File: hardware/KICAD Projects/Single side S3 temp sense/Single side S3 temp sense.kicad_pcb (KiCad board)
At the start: 2 copper layers, 39 parts, among them J1 TYPE-C-31-M-12, J2 DTF13-6P, SW1 PTS810_SJM_250_SMTR_LFS, SW2 PTS810_SJM_250_SMTR_LFS, U1 AMS1117-3.3, U2 ESP32-S3-WROOM-1, U3 MCP2515-I, U4 TJA1050DRG, X1 8MHz

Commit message: can template finished
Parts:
- removed D6: SK6812, LED_SMD:LED_SK6812_PLCC4_5.0x5.0mm_P3.2mm
- added REF**: MountingHole_3.2mm_M3, MountingHole:MountingHole_3.2mm_M3, F.Cu at (147.5, 102.5)
- added REF**: MountingHole_3.2mm_M3, MountingHole:MountingHole_3.2mm_M3, F.Cu at (87.9, 57.4)
- added REF**: MountingHole_3.2mm_M3, MountingHole:MountingHole_3.2mm_M3, F.Cu at (87.9, 103.6)
- added REF**: MountingHole_3.2mm_M3, MountingHole:MountingHole_3.2mm_M3, F.Cu at (147.5, 58.5)
- U5: moved to B.Cu
- moved R9 153.0 mm to (114.2, 69.5)
- moved R4 149.1 mm to (114.2, 71.2)
- moved C8 144.9 mm to (114.2, 68.0), turned to 180 degrees
- moved C7 144.9 mm to (114.2, 66.2), turned to 180 degrees
- moved C6 141.0 mm to (114.2, 72.8), turned to 180 degrees
- moved U2 123.6 mm to (126.1, 69.3)
- moved R6 122.9 mm to (138.8, 70.7), turned to 90 degrees
- moved C10 122.2 mm to (138.8, 67.2), turned to 90 degrees
- moved C11 122.0 mm to (116.2, 89.8), turned to 180 degrees
- moved U3 118.7 mm to (123.8, 96.8)
- moved R8 118.0 mm to (123.1, 89.5)
- moved R5 116.8 mm to (138.8, 78.5), turned to 90 degrees
- moved SW2 116.5 mm to (142.1, 69.0), turned to -90 degrees
- moved C9 115.3 mm to (138.8, 75.2), turned to 90 degrees
- moved SW1 111.3 mm to (142.1, 76.8), turned to -90 degrees
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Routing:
- net VCC_3V3: track 0.00 -> 94.7 mm, vias 0 -> 4
- net VCC_5V: track 0.00 -> 81.4 mm, vias 0 -> 2
- net GND: track 0.00 -> 80.7 mm, vias 0 -> 18
- net High: track 0.00 -> 78.9 mm
- net Low: track 0.00 -> 68.8 mm
- net SCL: track 0.00 -> 43.1 mm
- net CHIP_PU: track 0.00 -> 41.4 mm, vias 0 -> 3
- net Net-(U3-OSC2): track 0.00 -> 28.1 mm
- net SCK: track 0.00 -> 26.6 mm, vias 0 -> 2
- net D+: track 0.00 -> 25.4 mm
- net D-: track 0.00 -> 25.3 mm
- net SDA: track 0.00 -> 24.2 mm
- net Net-(U3-TXCAN): track 0.00 -> 23.7 mm
- net Net-(D1-A): track 0.00 -> 22.9 mm
- net Net-(U3-OSC1): track 0.00 -> 22.3 mm
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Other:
- board outline added: 78.9 x 54 mm

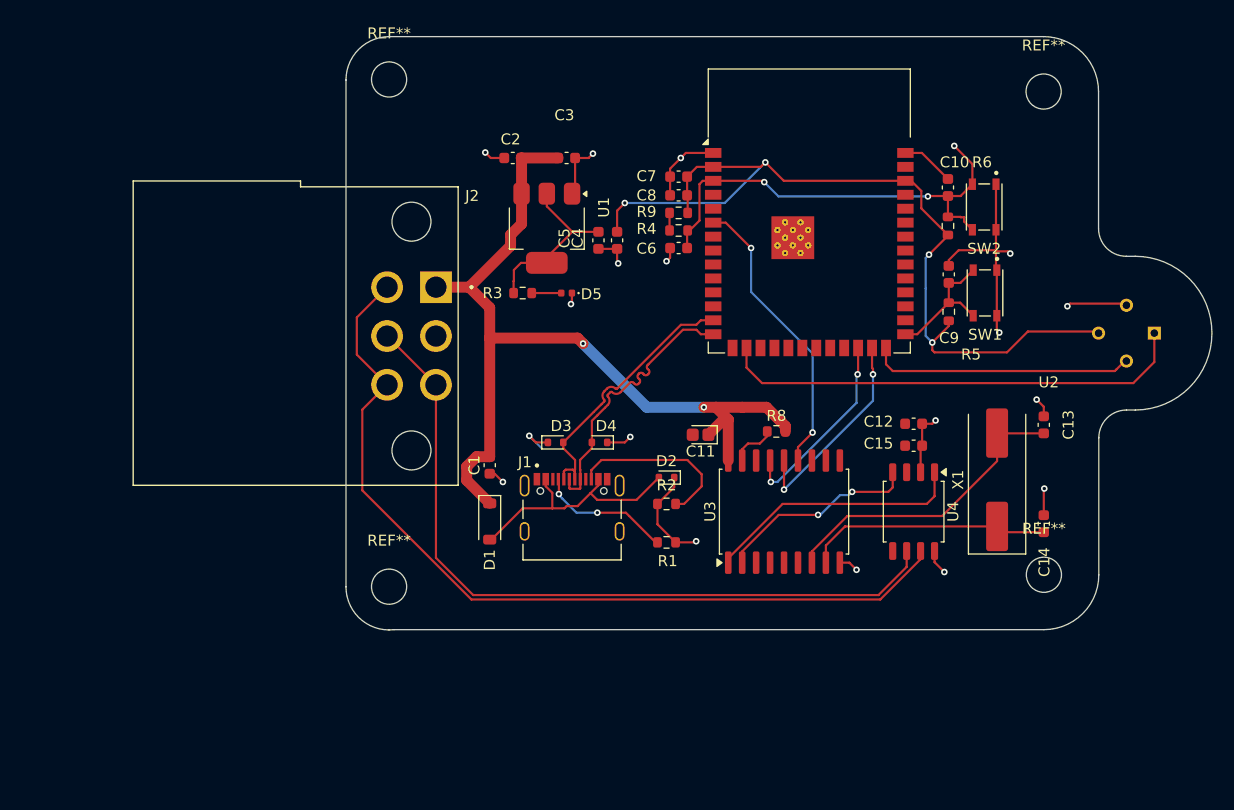
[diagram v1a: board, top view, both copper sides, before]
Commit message: finished the single side temp sense
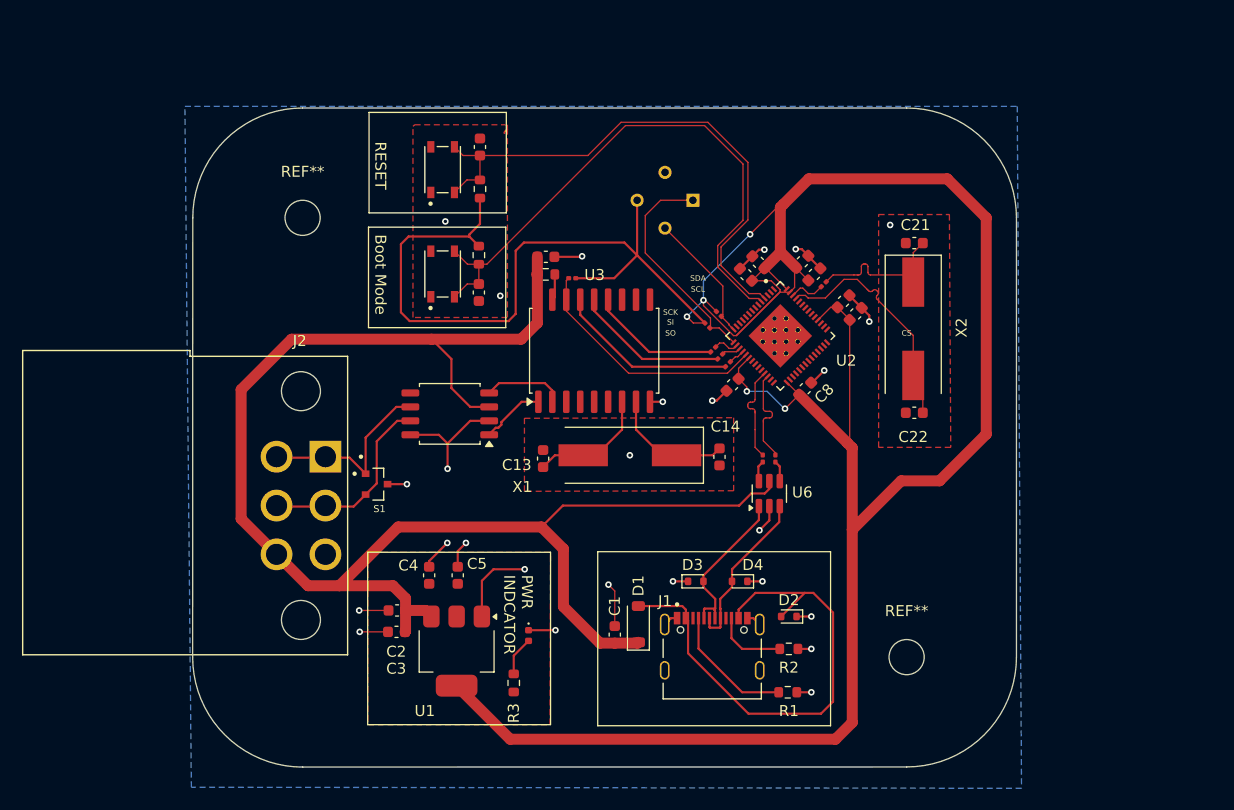
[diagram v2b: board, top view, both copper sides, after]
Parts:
- removed C11: 10uF/16V, Capacitor_Tantalum_SMD:CP_EIA-1608-08_AVX-J
- removed C15: 100nF, Capacitor_SMD:C_0603_1608Metric
- removed the REF** at (147.5, 102.5)
- removed the REF** at (87.9, 57.4)
- removed the REF** at (87.9, 103.6)
- removed the REF** at (147.5, 58.5)
- added C16: 100n, Capacitor_SMD:C_0603_1608Metric, F.Cu at (129.2, 77.6)
- added C17: 100n, Capacitor_SMD:C_0603_1608Metric, F.Cu at (119.2, 85.2)
- added C18: 1u, Capacitor_SMD:C_0603_1608Metric, F.Cu at (125.5, 74.0)
- added C19: 1u, Capacitor_SMD:C_0603_1608Metric, F.Cu at (121.5, 74.0)
- added C20: 10u, Capacitor_SMD:C_0603_1608Metric, F.Cu at (130.4, 78.7)
- added C21: 10pf, Capacitor_SMD:C_0603_1608Metric, F.Cu at (135.7, 72.3)
- added C22: 10pf, Capacitor_SMD:C_0603_1608Metric, F.Cu at (135.7, 87.8)
- added R10: 4.7K, Resistor_SMD:R_0201_0603Metric, F.Cu at (117.9, 78.8)
- added R11: 4.7K, Resistor_SMD:R_0201_0603Metric, F.Cu at (116.8, 79.8)
- added R12: 10k, Resistor_SMD:R_0201_0603Metric, F.Cu at (104.5, 75.5)
- added R13: 22, Resistor_SMD:R_0201_0603Metric, F.Cu at (121.9, 91.9)
- added R14: 22, Resistor_SMD:R_0201_0603Metric, F.Cu at (123.0, 91.9)
- added R15: 22, Resistor_SMD:R_0201_0603Metric, F.Cu at (127.5, 76.0)
- added R7: 33, Resistor_SMD:R_0201_0603Metric, F.Cu at (117.4, 82.0)
- added REF**: MountingHole_3.2mm_M3, MountingHole:MountingHole_3.2mm_M3, F.Cu at (80.0, 70.0)
- added REF**: MountingHole_3.2mm_M3, MountingHole:MountingHole_3.2mm_M3, F.Cu at (135.0, 110.0)
- added S1: PESD2CAN_215, 0_Custom:DIO_PESD2CAN_215, F.Cu at (86.7, 94.2)
- added U6: USBLC6-2SC6, Package_TO_SOT_SMD:SOT-23-6, F.Cu at (122.5, 95.1)
- added X2: 8MHz, Crystal:Crystal_SMD_HC49-SD, F.Cu at (135.6, 80.1)
- C6: value 1u -> 100n
- C7: value 10u -> 100n
- C8: value 0u1 -> 100n
- R4, R9: value 10k -> 33; footprint Resistor_SMD:R_0603_1608Metric -> Resistor_SMD:R_0201_0603Metric
- U2: value ESP32-S3-WROOM-1 -> ESP32-S3FN8; footprint RF_Module:ESP32-S3-WROOM-1 -> 0_Custom:IC_ESP32-S3
- moved SW2 49.4 mm to (92.8, 65.6), turned to 90 degrees
- moved SW1 49.4 mm to (92.8, 75.1), turned to 90 degrees
- moved C3 45.8 mm to (88.5, 107.7), turned to 180 degrees
- moved C13 45.7 mm to (101.9, 91.9)
- moved U5 43.7 mm to (113.0, 68.4)
- moved U4 43.2 mm to (93.4, 87.8), turned to 180 degrees
- moved R5 43.1 mm to (96.0, 73.4), turned to -90 degrees
- moved C9 42.8 mm to (96.0, 76.8), turned to -90 degrees
- moved C10 42.8 mm to (96.1, 63.5)
- moved R6 42.7 mm to (96.2, 67.4)
- moved C2 42.5 mm to (88.6, 105.8)
- moved U1 39.4 mm to (94.0, 109.5)
- moved C12 36.8 mm to (102.2, 73.5)
- moved R3 35.5 mm to (99.2, 112.3), turned to 90 degrees
- moved C4 35.0 mm to (91.5, 102.5), turned to 90 degrees
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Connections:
- C6 pad 1: CHIP_PU -> GND
- C6 pad 2: GND -> VCC_3V3
- C7 pad 1: VCC_3V3 -> GND
- C7 pad 2: GND -> VCC_3V3
- C8 pad 1: VCC_3V3 -> GND
- C8 pad 2: GND -> VCC_3V3
- J2 pad 1: VCC_5V -> Low
- J2 pad 2: GND -> High
- J2 pad 3: Low -> GND
- J2 pad 4: High -> VCC_5V
- J2 pad 5: Low -> High
- J2 pad 6: High -> Low
- R4 pad 1: ESP_3V3 -> SI
- R4 pad 2: CHIP_PU -> Net-(U2-GPIO12)
- R9 pad 1: ESP_3V3 -> SO
- R9 pad 2: VCC_3V3 -> Net-(U2-GPIO13)
- U2 pad 1: GND -> unconnected-(U2-LNA_IN-Pad1)
- U2 pad 12: RGB -> unconnected-(U2-GPIO7-Pad12)
- U2 pad 13: D- -> unconnected-(U2-GPIO8-Pad13)
- U2 pad 14: D+ -> SDA
- U2 pad 15: unconnected-(U2-IO3-Pad15) -> SCL
- U2 pad 16: SCL -> Net-(U2-GPIO11)
- U2 pad 17: CLK -> Net-(U2-GPIO12)
- U2 pad 18: CS -> Net-(U2-GPIO13)
- U2 pad 19: DC -> CS
- U2 pad 2: VCC_3V3 -> unconnected-(U2-VDD3P3-Pad2)_1
- U2 pad 20: RST -> VCC_3V3
- U2 pad 21: BL -> unconnected-(U2-XTAL_32K_P-Pad21)
- U2 pad 24: SO -> unconnected-(U2-GPIO18-Pad24)
- U2 pad 25: SI -> Net-(U2-GPIO19)
- U2 pad 26: SDA -> Net-(U2-GPIO20)
- U2 pad 27: GPI00 -> unconnected-(U2-GPIO21-Pad27)
- U2 pad 29: unconnected-(U2-IO36-Pad29) -> VCC_3V3
- U2 pad 3: CHIP_PU -> unconnected-(U2-VDD3P3-Pad2)
- U2 pad 38: VCC_3V3 -> unconnected-(U2-GPIO33-Pad38)
- U2 pad 4: unconnected-(U2-IO4-Pad4) -> CHIP_PU
- U2 pad 40: GND -> unconnected-(U2-GPIO35-Pad40)
- U2 pad 41: GND -> unconnected-(U2-GPIO36-Pad41)
- U2 pad 5: unconnected-(U2-IO5-Pad5) -> GPI00
- U2 pad 6: SCK -> unconnected-(U2-GPIO1-Pad6)
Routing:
- net VCC_3V3: track 94.7 -> 274.3 mm, vias 4 -> 5
- net High: track 78.9 -> 17.9 mm
- net VCC_5V: track 81.4 -> 140.1 mm, vias 2 -> 0
- net Low: track 68.8 -> 17.5 mm
- net GPI00: track 12.4 -> 53.6 mm
- net Net-(D1-A): track 22.9 -> 46.3 mm
- net SCL: track 43.1 -> 20.3 mm
- net CS: track 0.00 -> 22.5 mm
- net XTAL_N: track 0.00 -> 21.7 mm
- net Net-(U3-TXCAN): track 23.7 -> 5.90 mm
- net Net-(U3-OSC2): track 28.1 -> 11.1 mm
- net GND: track 80.7 -> 65.2 mm, vias 18 -> 26
- net SCK: track 26.6 -> 11.9 mm, vias 2 -> 0
- net Net-(C21-Pad1): track 0.00 -> 13.9 mm
- net SDA: track 24.2 -> 11.9 mm
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- added copper zone on B.Cu, net GND
- added copper zone on F.Cu, net GND
- added copper zone on F.Cu, net VCC_3V3
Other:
- board size 78.9 x 54 mm -> 75 x 60 mm
- board text added: "Boot Mode"
- board text added: "C3"
- board text added: "CS"
- board text added: "Designed by Connor Larson in Tucson, Arizona"
- board text added: "PWR INDCATOR"
- board text added: "RESET"
- board text added: "SCK"
- board text added: "SCL"
- board text added: "SDA"
- board text added: "SI"
- board text added: "SO"
- board text added: "Temperature Sensor REV 0"
